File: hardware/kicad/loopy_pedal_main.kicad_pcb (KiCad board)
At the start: 2 copper layers, 82 x 90 mm, 84 parts, among them J1 USB, J10 MOCO, J11 IND, J12 UNDO, J13 MODE, J14 TRACK1, J15 TRACK2, J16 TRACK3, J17 TRACK4, J18 CLEAR, J19 BANK, J2 9V, J3 RECPLAY, J4 STOP, J5 RING, J6 ICSP U1, J7 ICSP U2, J8 MIDI OUT, J9 MIDI IN, Q1 AO3401A, SW1 RST U1, SW2 RST U2, U1 ATmega328P-A, U10 74AHCT1G08, U2 ATmega16U2-A, U3 AP63203WU, U4 74AHCT1G125, U5 LM66100DCK, U6 LM66100DCK, U7 USBLC6-2SC6, U8 74AHCT1G125, U9 H11L1, Y1 16MHz, Y2 16MHz

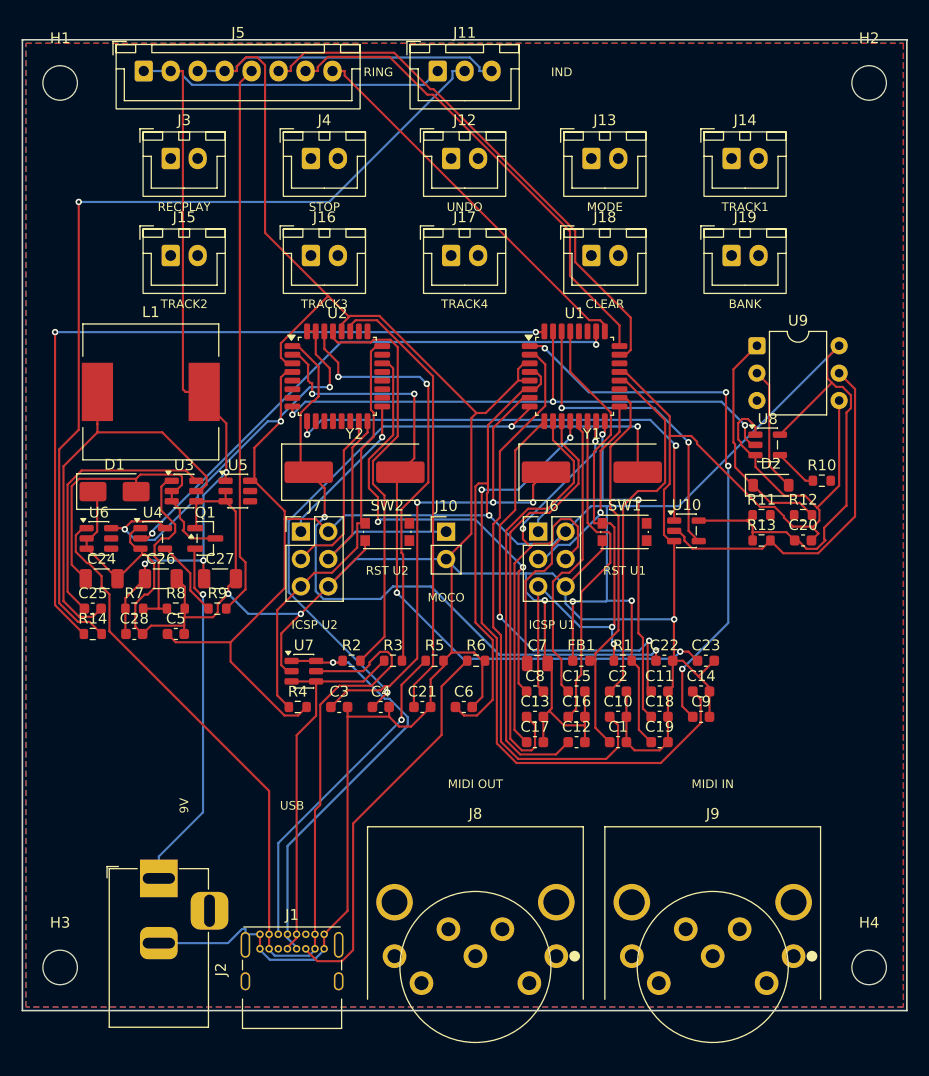
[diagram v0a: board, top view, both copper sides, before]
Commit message: fix(pcb): sync footswitch/MIDI nets, separate logic band, clean silk
The board file had drifted out of sync with main_board.net: all 10
footswitch headers (J3,J4,J12-J19) and both MIDI jacks (J8/J9) had no
nets on their signal pins, so they were unconnected copper and the
router silently treated them as nothing to route. Rebuilt the board
from the netlist so those connections are real and routed.

Placement/silk:
- push the logic zone (ATmega U1/U2 + SMD band) down to y31-73 and grow
  the board 82x90 -> 82x94 so there is a clear gap above the IC band
- even-space the RING (J5) / IND (J11) top connectors
- drop the footswitch grid for a 2.8 mm gap to the top connectors
- move all reference designators to the fab layer and keep the function
  names on silk; move edge-overhanging connector outlines to fab too
  (silk DRC warnings 102 -> 0)

Routed clean: 1003 segments, 63 vias, 2 GND pours, DRC 0 errors /
0 unconnected (nudged one via off an N$6 track to clear a router nick).

Regenerated the main-board fab package (gerbers+drill zip, CPL, BOM).

Co-Authored-By: Claude Opus 4.8 <noreply@anthropic.com>
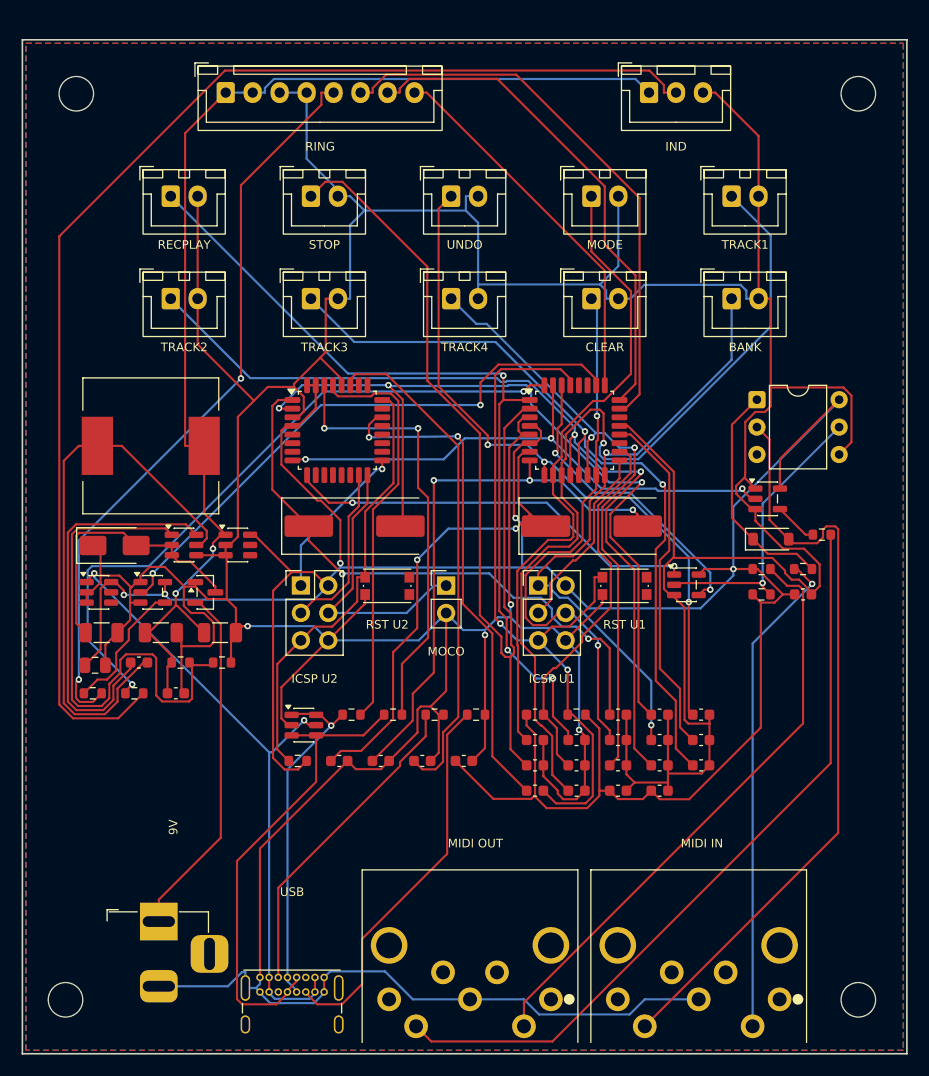
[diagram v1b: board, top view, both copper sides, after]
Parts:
- moved C5 43.5 mm to (85.2, 99.6)
- moved C7 41.0 mm to (36.7, 88.0)
- moved C6 19.7 mm to (89.1, 99.6)
- moved J11 19.7 mm to (88.1, 34.9)
- moved C19 18.2 mm to (70.9, 96.9)
- moved R9 14.0 mm to (36.5, 90.6)
- moved C15 13.4 mm to (92.9, 97.3)
- moved C9 11.7 mm to (81.4, 94.9)
- moved C8 9.20 mm to (77.5, 99.6)
- moved C2 8.92 mm to (92.9, 94.9)
- moved C10 8.92 mm to (77.5, 97.3)
- moved J5 7.86 mm to (48.9, 34.9)
- moved C13 7.86 mm to (81.4, 99.6)
- moved C14 7.86 mm to (89.1, 97.3)
- moved C17 7.70 mm to (85.2, 94.9)
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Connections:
- J12 pad 1: (no net) -> SW_UNDO
- J12 pad 2: (no net) -> GND
- J13 pad 1: (no net) -> SW_MODE
- J13 pad 2: (no net) -> GND
- J14 pad 1: (no net) -> SW_TRACK1
- J14 pad 2: (no net) -> GND
- J15 pad 1: (no net) -> SW_TRACK2
- J15 pad 2: (no net) -> GND
- J16 pad 1: (no net) -> SW_TRACK3
- J16 pad 2: (no net) -> GND
- J17 pad 1: (no net) -> SW_TRACK4
- J17 pad 2: (no net) -> GND
- J18 pad 1: (no net) -> SW_CLEAR
- J18 pad 2: (no net) -> GND
- J19 pad 1: (no net) -> SW_BANK
- J19 pad 2: (no net) -> GND
- J3 pad 1: (no net) -> SW_RECPLAY
- J3 pad 2: (no net) -> GND
- J4 pad 1: (no net) -> SW_STOP
- J4 pad 2: (no net) -> GND
- J8 pad 2: (no net) -> GND
- J8 pad 4: (no net) -> N$18
- J8 pad 5: (no net) -> N$17
- J9 pad 2: (no net) -> GND
- J9 pad 4: (no net) -> N$19
- J9 pad 5: (no net) -> N$21
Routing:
- net GND: track 435.8 -> 571.3 mm
- net N$17: track 0.00 -> 70.9 mm
- net N$21: track 11.6 -> 71.0 mm
- net N$18: track 0.00 -> 55.0 mm
- net N$19: track 0.00 -> 45.5 mm, vias 0 -> 1
- net SW_TRACK3: track 27.3 -> 72.8 mm, vias 0 -> 2
- net SW_TRACK1: track 39.8 -> 82.2 mm, vias 0 -> 1
- net SW_STOP: track 54.2 -> 89.7 mm
- net VBUS: track 91.9 -> 58.7 mm, vias 0 -> 2
- net IND_DATA_OUT: track 84.3 -> 117.5 mm, vias 1 -> 0
- net FB: track 16.6 -> 49.4 mm
- net +5V: track 280.6 -> 250.0 mm, vias 6 -> 5
- net SW_TRACK4: track 30.5 -> 58.6 mm, vias 0 -> 2
- net SW_RECPLAY: track 52.3 -> 77.7 mm, vias 4 -> 3
- net SW_TRACK2: track 60.3 -> 85.3 mm
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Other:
- board size 82 x 90 mm -> 82 x 94 mm
